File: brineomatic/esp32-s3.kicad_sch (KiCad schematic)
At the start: 47 parts, among them J3 USB_TYPE_C_16PIN, Q1 FDC6330L, Q2 S8050, Q3 S8050, SW1 RESET, SW2 BOOT, U1 ESP32-S3-WROOM-1-N16R8, U2 USBLC6-2SC6, U3 XC6210B332MR, U4 CH334F, U5 CH343P, Y1 12Mhz, Y2 32.768kHz

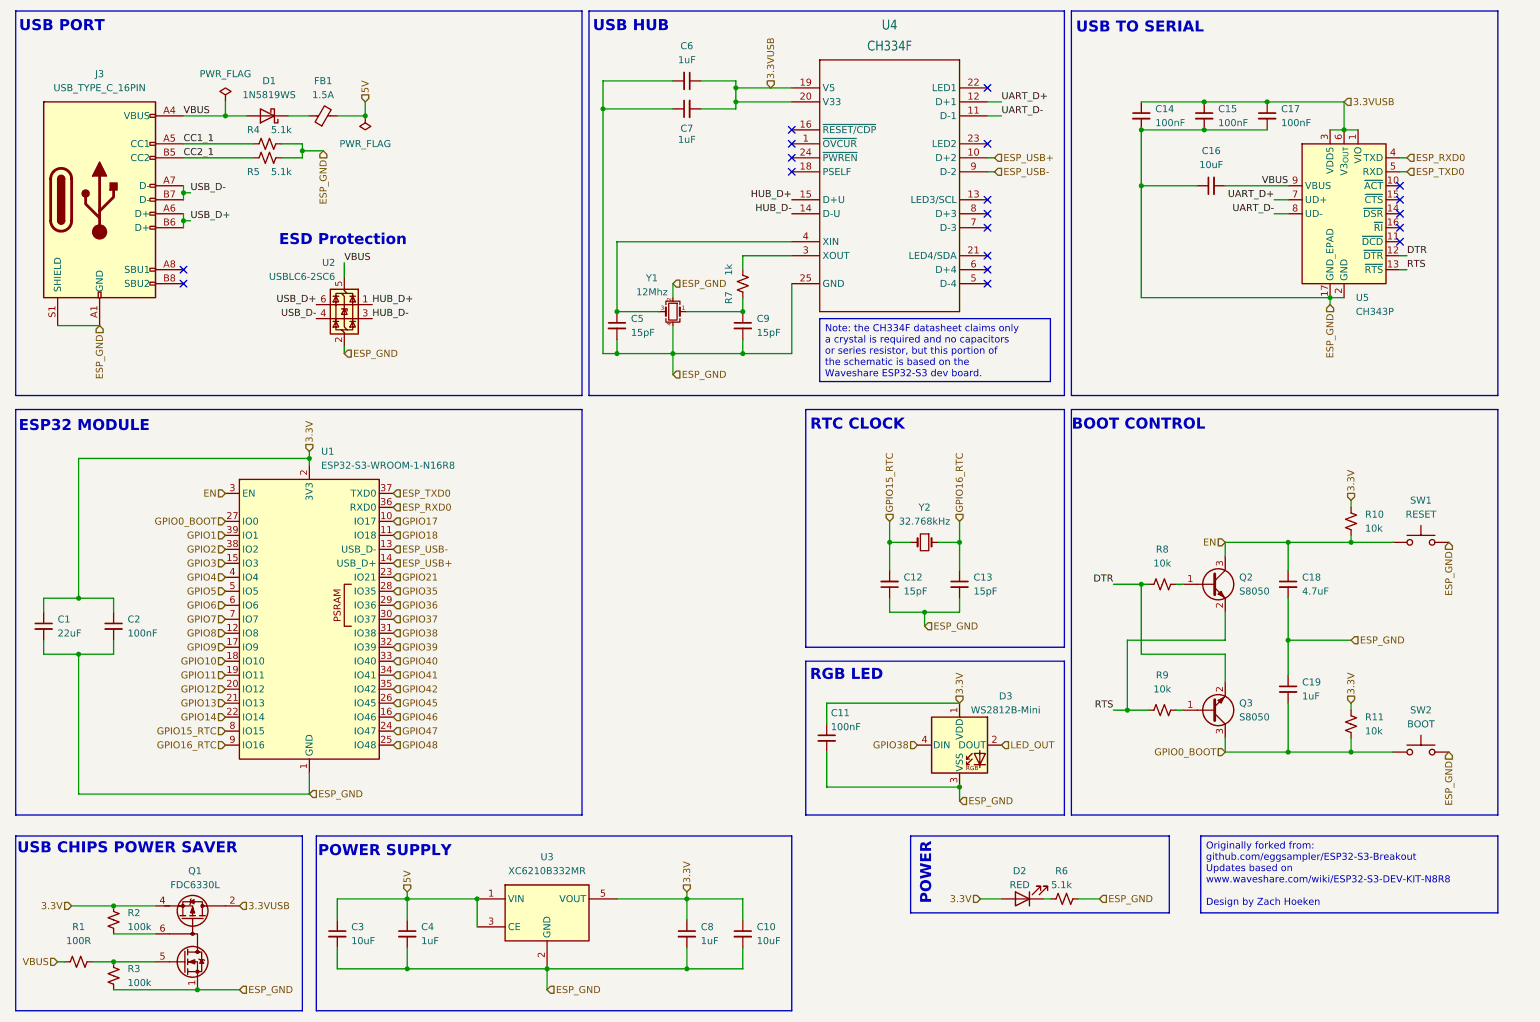
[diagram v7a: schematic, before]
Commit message: via stitching, a couple minor changes, i think its ready for production
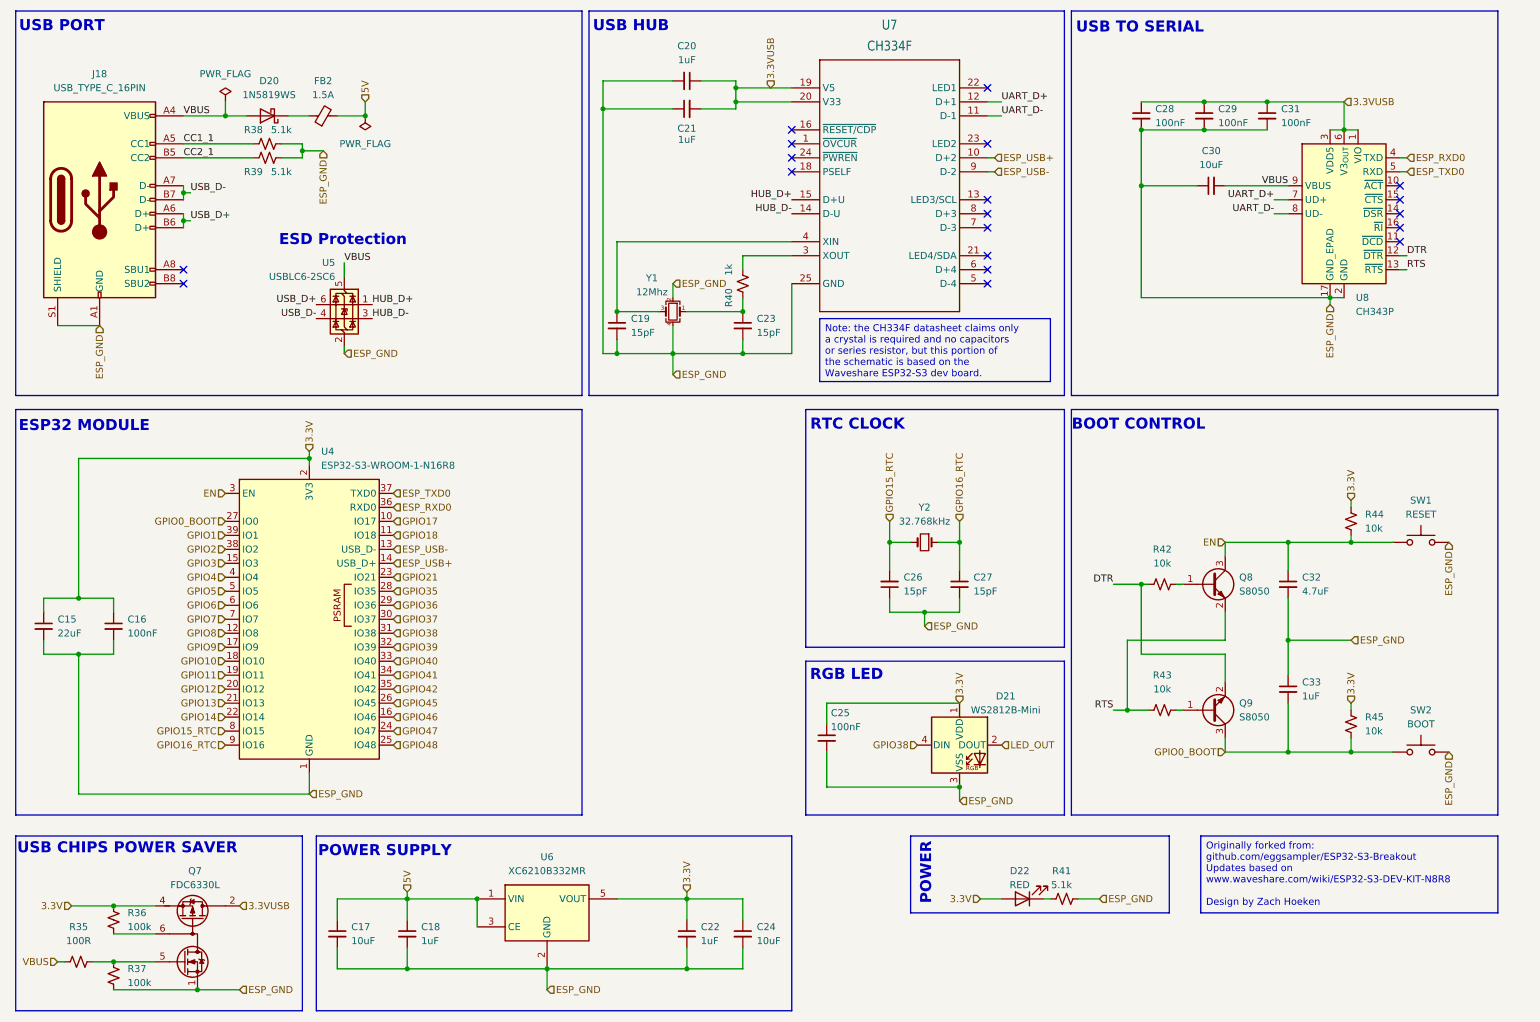
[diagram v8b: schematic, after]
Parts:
- renumbered C1 to C15, C2 to C16, C3 to C17, C4 to C18, C5 to C19, C6 to C20, C7 to C21, C8 to C22, C9 to C23, C10 to C24, C11 to C25, C12 to C26, C13 to C27, C14 to C28, C15 to C29, C16 to C30, C17 to C31, C18 to C32, C19 to C33, D1 to D20, D3 to D21, D2 to D22, FB1 to FB2, J3 to J18, Q1 to Q7, Q2 to Q8, Q3 to Q9, R1 to R35, R2 to R36, R3 to R37, R4 to R38, R5 to R39, R7 to R40, R6 to R41, R8 to R42, R9 to R43, R10 to R44, R11 to R45, U1 to U4, U2 to U5, U3 to U6, U4 to U7, U5 to U8
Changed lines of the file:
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@@
 		(dnp no)
 		(fields_autoplaced yes)
-		(property "Reference" "Q3"
+		(property "Reference" "Q9"
 			(at 236.22 139.6999 0)
 			(effects
@@
 		(dnp no)
 		(fields_autoplaced yes)
-		(property "Reference" "#FLG03"
+		(property "Reference" "#FLG011"
 			(at 77.47 34.925 0)
 			(effects
@@
 		(dnp no)
 		(fields_autoplaced yes)
-		(property "Reference" "U4"
+		(property "Reference" "U7"
 			(at 172.72 16.51 0)
 			(effects
@@
 		(on_board yes)
 		(dnp no)
-		(property "Reference" "R5"
+		(property "Reference" "R39"
 			(at 57.15 43.18 90)
 			(effects
@@
 		(dnp no)
 		(fields_autoplaced yes)
-		(property "Reference" "C4"
+		(property "Reference" "C18"
 			(at 87.63 180.3462 0)
 			(effects
@@
 		(on_board yes)
 		(dnp no)
-		(property "Reference" "D2"
+		(property "Reference" "D22"
 			(at 196.342 170.18 0)
 			(effects
@@
 		(dnp no)
 		(fields_autoplaced yes)
-		(property "Reference" "C1"
+		(property "Reference" "C15"
 			(at 21.59 124.4662 0)
 			(effects
@@
 		(on_board yes)
 		(dnp no)
-		(property "Reference" "R6"
+		(property "Reference" "R41"
 			(at 203.962 170.18 90)
 			(effects
@@
 		(dnp no)
 		(fields_autoplaced yes)
-		(property "Reference" "C13"
+		(property "Reference" "C27"
 			(at 187.96 116.8462 0)
 			(effects
@@
 		(on_board yes)
 		(dnp no)
-		(property "Reference" "C9"
+		(property "Reference" "C23"
 			(at 148.59 69.8562 0)
 			(effects
@@
 		(dnp no)
 		(fields_autoplaced yes)
-		(property "Reference" "R8"
+		(property "Reference" "R42"
 			(at 222.25 111.76 90)
 			(effects
@@
 		(dnp no)
 		(fields_autoplaced yes)
-		(property "Reference" "R1"
+		(property "Reference" "R35"
 			(at 25.4 180.34 90)
 			(effects
@@
 		(dnp no)
 		(fields_autoplaced yes)
-		(property "Reference" "C15"
+		(property "Reference" "C29"
 			(at 232.41 31.7562 0)
 			(effects
@@
 		(dnp no)
 		(fields_autoplaced yes)
-		(property "Reference" "C18"
+		(property "Reference" "C32"
 			(at 247.65 116.8462 0)
 			(effects
@@
 		(on_board yes)
 		(dnp no)
-		(property "Reference" "C6"
+		(property "Reference" "C20"
 			(at 135.8836 20.32 90)
 			(effects
@@
 		(dnp no)
 		(fields_autoplaced yes)
-		(property "Reference" "U5"
+		(property "Reference" "U8"
 			(at 257.4133 66.04 0)
 			(effects
@@
 		(dnp no)
 		(fields_autoplaced yes)
-		(property "Reference" "U3"
+		(property "Reference" "U6"
 			(at 110.49 167.64 0)
 			(effects
@@
 		(dnp no)
 		(fields_autoplaced yes)
-		(property "Reference" "U2"
+		(property "Reference" "U5"
 			(at 72.0089 59.69 0)
 			(effects
@@
 		(dnp no)
 		(fields_autoplaced yes)
-		(property "Reference" "C19"
+		(property "Reference" "C33"
 			(at 247.65 135.8962 0)
 			(effects
@@
 		(on_board yes)
 		(dnp no)
-		(property "Reference" "C7"
+		(property "Reference" "C21"
 			(at 135.89 35.306 90)
 			(effects
@@
 		(dnp no)
 		(fields_autoplaced yes)
-		(property "Reference" "C2"
+		(property "Reference" "C16"
 			(at 34.29 124.4662 0)
 			(effects
@@
 		(dnp no)
 		(fields_autoplaced yes)
-		(property "Reference" "R9"
+		(property "Reference" "R43"
 			(at 222.25 134.62 90)
 			(effects
@@
 		(on_board yes)
 		(dnp no)
-		(property "Reference" "D3"
+		(property "Reference" "D21"
 			(at 193.802 138.43 0)
 			(effects
@@
 		(dnp no)
 		(fields_autoplaced yes)
-		(property "Reference" "Q1"
+		(property "Reference" "Q7"
 			(at 46.5455 170.18 0)
 			(effects
@@
 		(on_board yes)
 		(dnp no)
-		(property "Reference" "C14"
+		(property "Reference" "C28"
 			(at 220.98 31.7562 0)
 			(effects
@@
 		(on_board yes)
 		(dnp no)
-		(property "Reference" "R7"
+		(property "Reference" "R40"
 			(at 143.51 66.04 90)
 			(effects
@@
 		(dnp no)
 		(fields_autoplaced yes)
-		(property "Reference" "C5"
+		(property "Reference" "C19"
 			(at 125.73 69.8562 0)
 			(effects
@@
 		(dnp no)
 		(fields_autoplaced yes)
-		(property "Reference" "C3"
+		(property "Reference" "C17"
 			(at 74.93 180.3462 0)
 			(effects
@@
 		(dnp no)
 		(fields_autoplaced yes)
-		(property "Reference" "R3"
+		(property "Reference" "R37"
 			(at 34.29 187.9599 0)
 			(effects
@@
 		(dnp no)
 		(fields_autoplaced yes)
-		(property "Reference" "C17"
+		(property "Reference" "C31"
 			(at 243.84 31.7562 0)
 			(effects
@@
 		(dnp no)
 		(fields_autoplaced yes)
-		(property "Reference" "FB1"
+		(property "Reference" "FB2"
 			(at 69.8119 26.67 90)
 			(effects
@@
 		(dnp no)
 		(fields_autoplaced yes)
-		(property "Reference" "C10"
+		(property "Reference" "C24"
 			(at 148.59 180.3462 0)
 			(effects
@@
 		(on_board yes)
 		(dnp no)
-		(property "Reference" "C11"
+		(property "Reference" "C25"
 			(at 162.052 141.478 0)
 			(effects
@@
 		(dnp no)
 		(fields_autoplaced yes)
-		(property "Reference" "U1"
+		(property "Reference" "U4"
 			(at 69.4533 93.98 0)
 			(effects
@@
 		(dnp no)
 		(fields_autoplaced yes)
-		(property "Reference" "J3"
+		(property "Reference" "J18"
 			(at 29.21 25.4 0)
 			(effects
@@
 		(dnp no)
 		(fields_autoplaced yes)
-		(property "Reference" "#FLG02"
+		(property "Reference" "#FLG010"
 			(at 52.07 28.575 0)
 			(effects
@@
 		(dnp no)
 		(fields_autoplaced yes)
-		(property "Reference" "Q2"
+		(property "Reference" "Q8"
 			(at 236.22 116.8399 0)
 			(effects
@@
 		(dnp no)
 		(fields_autoplaced yes)
-		(property "Reference" "C16"
+		(property "Reference" "C30"
 			(at 231.1463 39.37 90)
 			(effects
@@
 		(dnp no)
 		(fields_autoplaced yes)
-		(property "Reference" "R11"
+		(property "Reference" "R45"
 			(at 259.08 142.2399 0)
 			(effects
@@
 		(dnp no)
 		(fields_autoplaced yes)
-		(property "Reference" "D1"
+		(property "Reference" "D20"
 			(at 60.0075 26.67 0)
 			(effects
@@
 		(on_board yes)
 		(dnp no)
-		(property "Reference" "R4"
+		(property "Reference" "R38"
 			(at 57.15 35.56 90)
 			(effects
@@
 		(dnp no)
 		(fields_autoplaced yes)
-		(property "Reference" "R2"
+		(property "Reference" "R36"
 			(at 34.29 177.7999 0)
 			(effects
@@
 		(dnp no)
 		(fields_autoplaced yes)
-		(property "Reference" "C8"
+		(property "Reference" "C22"
 			(at 138.43 180.3462 0)
 			(effects
@@
 		(dnp no)
 		(fields_autoplaced yes)
-		(property "Reference" "C12"
+		(property "Reference" "C26"
 			(at 175.26 116.8335 0)
 			(effects
@@
 		(dnp no)
 		(fields_autoplaced yes)
-		(property "Reference" "R10"
+		(property "Reference" "R44"
 			(at 259.08 105.4099 0)
 			(effects
